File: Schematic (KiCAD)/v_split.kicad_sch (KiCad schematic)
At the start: 109 parts, among them P1 INVERT, P10 NAND_2, P11 NAND_2, P12,13,18,19,25,26 Reg 3 DFF-Reset, P14 INVERT, P15 T-FF Preload, P16 NAND_2, P17 NAND_2, P2 NOR_2, P20 INVERT, P21 T-FF Preload, P22 BUFFER, P23 NAND_2, P24 NAND_2, P28 BUFFER, P3 INVERT, P4 INVERT, P6 Reg 2 DFF-Reset N, P8 INVERT, P9 T-FF Preload, T1 INVERT, T10 INVERT, T12 T-FF Preload, T13 INVERT, T14 INVERT, T15 T-FF Preload, T16 INVERT, T17 INVERT, T18 T-FF Preload, T19 INVERT, T2 INVERT, T20 INVERT, T21 T-FF Preload, T22 INVERT, T23 INVERT, T24 T-FF Preload, T25 INVERT, T26 INVERT, T27 T-FF Preload, T28 INVERT, T29 INVERT, T3 NAND_2, T30 T-FF Preload, T31 INVERT, T4 JK-FF Reset, T5 BUFFER, T6 INVERT, T7 INVERT, T8 T-FF Preload, T9 INVERT, X1 INVERT, X2 NAND_2

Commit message: - Lots of additional comments and signal name improvements.  - "Don't know what this is yet but it is important" section of the pulse channels:    - I worked out the logic and it is a 4-bit binary up-counter with preload, made from gates and D-latches instead of T-flip-flops.    - It is extremely similar to the envelope counter, but takes twice the die space and much more traces.    - None of its outputs go anywhere else, so I believe that it has no actual function.    - It seems to be a previous attempt at making the envelope counter and it got disconnected and left in.    - Each pulse channel has its own copy and I moved both of them to the "Artifacts" sheet.    - The wasted space amounts to about half of one of the large columns on the left side of the die.  - A couple of "OAI2" cells that noted "unclear order": I determined the correct order of the inputs based on several others which were known.  - Deduced the purpose of the 2 separate methods of scanline detection:    - The one looking for 3 consecutive reads finds the start of a scanline.    - The one counting PPU /RD to find PPU cycle 336, finds the end of the scanline.    - I moved these beside each other on the same sheet for clarity.  - A66.5 Changed from Nand to Nor in order to make sense.  - Basic test mode:    - Pin 92: Active low, enables test mode.    - Pin 29: In test mode, it gives external control of "Scanline Start Detection", which is normally done with the familiar 3 matching PPU reads.  When not in test mode, the pin has no function.    - Pin 30: In test mode, it gives external control of "Scanline End Detection", which is normally done by counting PPU /RD to find PPU cycle 336.  It also gives control of "Pulse Length Clock" when in test mode.  When not in test mode, the pin has no function.    - Pin 98/SL3: In test mode, it gives external control of "Pulse Timer Clock".  Whether or not in test mode, this pin low makes the MMC5 pretend $5104 had not yet been written since reset, probably as a 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
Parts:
- removed P1, P3, P4, R7, R8, S5, S6, X1: INVERT, symbol MMC5:INVERT
- removed P2: NOR_2, symbol MMC5:NOR_2
- removed R1: AOI_2, symbol MMC5:AOI_2
- removed R6, X2: NAND_2, symbol MMC5:NAND_2
- removed T4: JK-FF Reset, symbol MMC5:JK-FF_Reset
- removed T5: BUFFER, symbol MMC5:BUFFER
- added N3, N4: NAND_2, symbol MMC5:NAND_2
- added N5: XNOR_2, symbol MMC5:XNOR_2
- added T4: D-FF-SR, symbol MMC5:D-FF-SR
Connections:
- net $5200.6{P6} is gone; now on net /Reset_Detect{N2}: P6. (/Q1)
- net $5200.7{P6} is gone; now on net /Reset_Detect{N2}: P6. (/Q1)
- net +PPU_Fetch_Count.5{S25} is gone; now on net +PPU_Fetch_Counter.7{S29}: S4. (X)
- net Increment_PPU_Fetch_Count{S6} is gone; now on net /Reset_Detect{R14}: R4. (Q1)
- net R4.Q1 is gone; now on net /Reset_Detect{R14}: R4. (Q1)
- net V-Split_Scanline_Detected{P3} is gone; now on net Scanline_End_Detected{P3}: P22. (X), T8. (/Q)
- net V-Split_Scanline_Detected{T5} is gone; now on net Scanline_End_Detected{T5}: T3. (X)
- net V-Split_Side_Being_Rendered{V7} is gone; now on an unnamed net: V7. (X)
- net /PPU_Fetch_Count.4{S23} is gone; now on net /PPU_Fetch_Counter.4{S23}: S3. (X)
- net +PPU_Fetch_Counter.2{S18}: now also S3. (X), S4. (X)
- net +PPU_Fetch_Counter.5{S25}: now also S4. (X)
- net +PPU_Fetch_Counter.7{S29}: now also S3. (X)
- net /V-Split_Scanline=239{S30}: now also T4. (/Q)
- net at V4. (X): now also V5. (X); no longer V6. (X)
- net at V9. (X): now also V11. (X); no longer V4. (X)
- net at R27. (/Q): now also R26. (X)
- net at R26. (X): now also R29. (X); no longer R27. (/Q)
- net at P9. (/Q): now also P8. (X); no longer P10. (X)
- net at T2. (X): now also T1. (X); no longer T3. (X)
- net Scanline_End_Detected{T5}: now reaches T3. (X)
- net Scanline_End_Detected{T5}: now also T4. (/Q)
- net at P28. (X): now also R26. (X); no longer P12,13,18,19,25,26. (Q2)
- net at T20. (X): now also T21. (/Q); no longer V27. (X)
- net at T21. (/Q): now also V28. (X), V29. (X); no longer T20. (X)
- net at P21. (/Q): no longer P22. (X)
- net at T14. (X): now also T15. (/Q); no longer V19. (X)
- net at V7. (X): now also N4. (X); no longer V8. (/Q)
- net at T29. (X): now also V36. (X); no longer T30. (/Q)
- net at P15. (/Q): now also P20. (X), P21. (/Q); no longer P16. (X)
- net at V11. (X): now also V10. (X); no longer V12. (X)
- net at T26. (X): now also T27. (/Q); no longer V33. (X)
- net at T27. (/Q): no longer T26. (X)
- net /PPU_Fetch_Counter.4{S23}: now reaches S3. (X)
- net /PPU_Fetch_Counter.4{S23}: no longer R4. (Q1)
- net at T12. (/Q): now also T8. (/Q), T9. (X)
- net at T10. (X): now also V16. (X); no longer T12. (/Q)
- net at T30. (/Q): now also V37. (X), V38. (X); no longer T31. (X)
- net at T23. (X): now also V30. (X); no longer T24. (/Q)
- net at T15. (/Q): no longer T14. (X)
- net at BH32. (X): now also BH31. (X)
- net at T7. (X): now also T8. (/Q); no longer V13. (X)
- net Scanline_End_Detected{P3}: now reaches T8. (/Q)
- net Scanline_End_Detected{P3}: now also N3. (X); no longer T7. (X)
- net at T18. (/Q): now also T17. (X)
- net at T17. (X): now also V22. (X); no longer T18. (/Q)
- removed net +PPU_Fetch_Count.0{S10}: S3. (X), S4. (X)
- removed net +PPU_Fetch_Count.1{S13}: S3. (X), S4. (X)
- removed net +PPU_Fetch_Count.2{S18}: S3. (X), S4. (X)
- removed net +PPU_Fetch_Count.7{S29}: S3. (X), S4. (X)
- new net: N1. (X), P6. (/Q1)
- new net: V4. (X), V6. (X)
- new net: V3. (X), V4. (X)
- new net: V4. (X), V9. (X)
- new net: R27. (/Q), R28. (X)
- new net: R27. (/Q), R29. (X)
- new net: P10. (X), P9. (/Q)
- new net: P10. (X), P11. (X), P9. (/Q)
- new net: T3. (X), T4. (/Q)
- new net: BH28. (X), T4. (/Q)
- new net: BH32. (X), T4. (/Q)
- new net: T2. (X), T3. (X)
- new net: T18. (/Q), T19. (X), T21. (/Q)
- new net: T15. (/Q), T16. (X), T18. (/Q)
- new net: V6. (X), W2. (Q4)
- new net: P12,13,18,19,25,26. (Q2), P28. (X)
- new net: P12,13,18,19,25,26. (Q2), P17. (X)
- new net: P11. (X), P12,13,18,19,25,26. (Q2)
- new net: P12,13,18,19,25,26. (Q2), P24. (X)
- new net: P14. (X), P15. (/Q), P9. (/Q)
- new net: T20. (X), V27. (X)
- new net: T27. (/Q), V34. (X), V35. (X)
- new net: V33. (X), V34. (X)
- new net: P21. (/Q), P22. (X)
- new net: V19. (X), V20. (X)
- new net: T14. (X), V19. (X)
- new net: V7. (X), V8. (/Q)
- new net: V27. (X), V28. (X)
- new net: V3. (X), W2. (Q4)
- new net: T29. (X), T30. (/Q)
- new net: P15. (/Q), P16. (X), P17. (X)
- new net: P15. (/Q), P16. (X)
- new net: T18. (/Q), V23. (X), V26. (X)
- new net: V26. (X), W3,V24,V25,V41. (Q7)
- new net: V8. (/Q), V9. (X)
- new net: N3. (X), N4. (X), N5. (X)
- new net: V35. (X), W3,V24,V25,V41. (Q7)
- new net: V11. (X), V12. (X)
- new net: V12. (X), W2. (Q4)
- new net: P21. (/Q), P23. (X)
- new net: P21. (/Q), P23. (X), P24. (X)
- new net: T24. (/Q), T25. (X), T27. (/Q)
- new net: T26. (X), V33. (X)
- new net: T15. (/Q), V20. (X), V21. (X)
- new net: R4. (Q1), S4. (X)
- new net: R4. (Q1), S3. (X)
- new net: T12. (/Q), V17. (X), V18. (X)
- new net: T12. (/Q), T13. (X), T15. (/Q)
- new net: T10. (X), T12. (/Q)
- new net: V22. (X), V23. (X)
- new net: V18. (X), W3,V24,V25,V41. (Q7)
- new net: T30. (/Q), T31. (X)
- new net: T23. (X), T24. (/Q)
- new net: T21. (/Q), T22. (X), T24. (/Q)
- new net: BH29. (X), BH30. (X)
- new net: T27. (/Q), T28. (X), T30. (/Q)
- new net: V16. (X), V17. (X)
- new net: T7. (X), V13. (X)
- new net: V13. (X), V14. (X)
- new net: V5. (X), W2. (Q4)
- new net: V36. (X), V37. (X)
- new net: T24. (/Q), V31. (X), V32. (X)
- new net: V32. (X), W3,V24,V25,V41. (Q7)
- new net: V29. (X), W3,V24,V25,V41. (Q7)
- new net: T6. (X), V11. (X)
- new net: V30. (X), V31. (X)
- new net: N3. (X), N4. (X)
- new net: V38. (X), W3,V24,V25,V41. (Q7)
- new net: T8. (/Q), V14. (X), V15. (X)
- new net: V2. (X), W2. (Q4)
- new net: V21. (X), W3,V24,V25,V41. (Q7)
- new net: V15. (X), W3,V24,V25,V41. (Q7)
- new net: V10. (X), W2. (Q4)
- new net +$5200.6_V-Split_Side_Right{P6}: N5. (X), P6. (/Q1)
- new net +$5200.7_V-Split_Enable{P6}: P6. (/Q1)
- new net +PPU_Cycle_336{R4}: R4. (Q1)
- new net +PPU_Fetch_Counter.0{S10}: S3. (X), S4. (X)
- new net +PPU_Fetch_Counter.1{S13}: S3. (X), S4. (X)
- new net Increment_Scanline_Fetch_Count{S6}: R4. (Q1)
- new net PPU_Fetch_Count_Match_0{R4}: R4. (Q1)
- new net V-Split_Rendering{N5}: N5. (X)
- now unconnected: P21. (/Q), P21. (/Q), P21. (/Q), T15. (/Q), T15. (/Q), T15. (/Q), T24. (/Q), T24. (/Q), T24. (/Q), T27. (/Q), T27. (/Q), T27. (/Q)
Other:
- note added: "0=prevent reload 1=allow reload"
- note added: "Comparing the fetch counter, shifted right by 2, to the $5200 V-Split H-threshold, Every 4 fetches = 1 tile. The match at V9..V7 holds true only for 1 fetch, so it is latched by N3/N4 until a new scanline is detected."
- note added: "Q1 = 1 at PPU cycle 336 for incrementing V-split scanline counter. Logic from S4: Value 1x1xx111, when incrementing, First triggered at 10100111=0xA7=167. Because fetch count clocks the latch, 167+1 = 168. Since PPU has 2 cycles per fetch, 168*2=336 cycles. This aligns with "unused NT fetches" at the end of the scanline."
- note added: "S3 = 0 at these values: 135, 143 (cycle 272, 288) 167, 175 (cycle 336, 352) 199, 207 (cycle 400, 416) 231, 239 (cycle 464, 480) These values don't make much sense, but it seems it should correlate to sprite pattern fetches"
- note added: "XNor N5 selects the left/right side based on $5002.6"
- note removed: "I am guessing this is any PPU fetch excluding sprites"
- note removed: "This Flip-Flop is unknown and J & K are complete guesses. May need swapping or inverting J & K and Q & /Q."
- note removed: "This cell has unknown logic"
- moved on the sheet: BH28, BH29, BH30, BH31, BH32, N1, P6, R4, S3, S30, S4

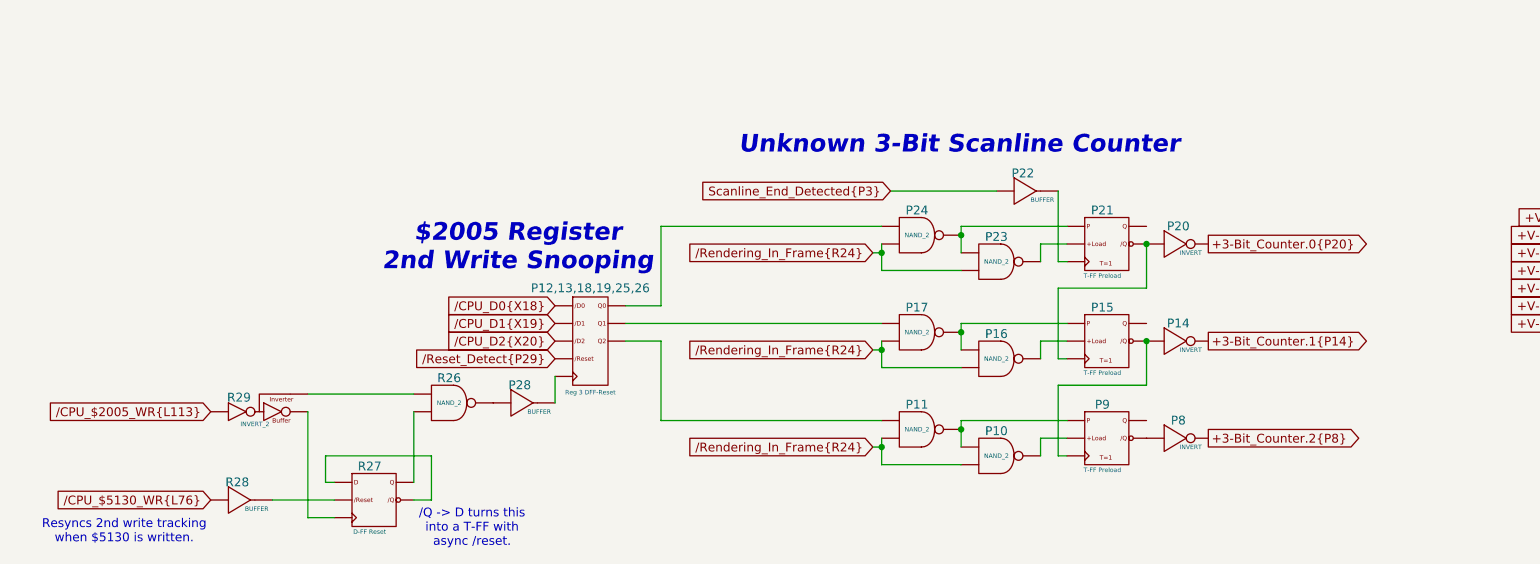
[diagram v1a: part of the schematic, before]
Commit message: I fixed 2 errors in the letterless MMC5 tracing:
1. BK5 is a NAND-4 gate.  It was thought to be NAND-3 before.
2.  BL83 and BL96 signals got swapped here before.  They actually cross each other:

BL83 = "PPU_RW_Mode_%0x_Access"
BL96 = "+ExRAM_Mode_$0x"

This propagated out to several changes in the schematic.
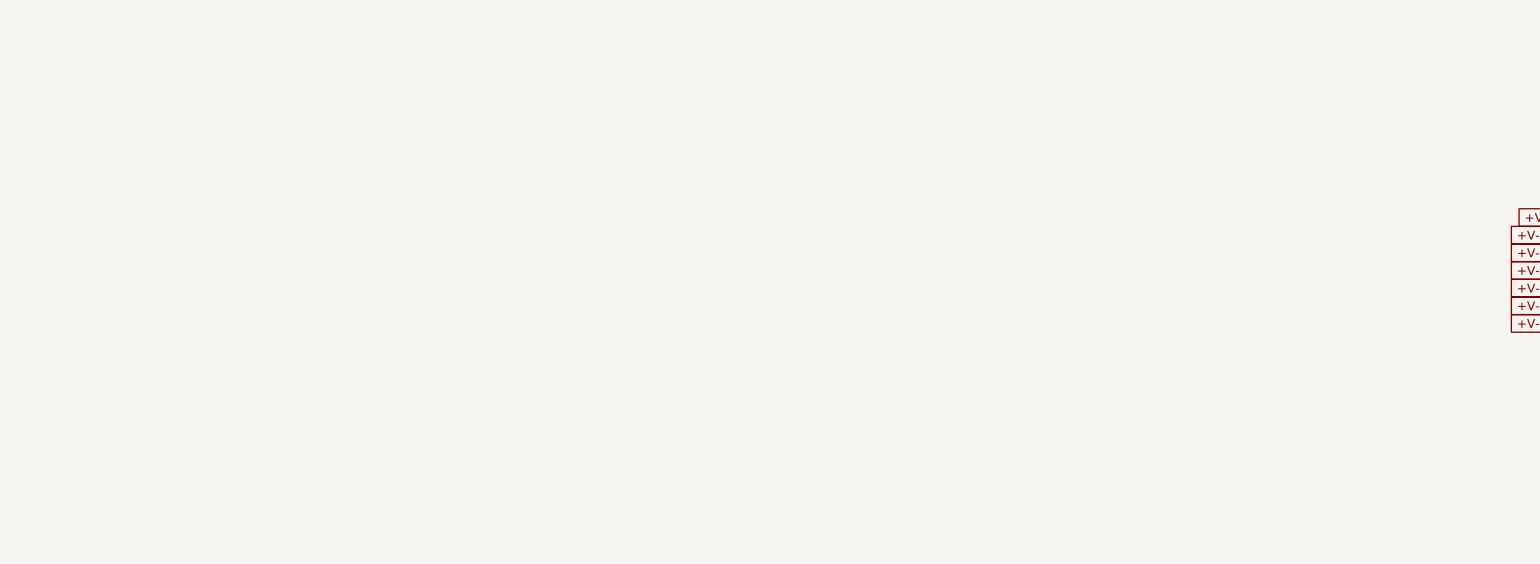
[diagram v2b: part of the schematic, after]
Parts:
- removed P10, P11, P16, P17, P23, P24, R26: NAND_2, symbol MMC5:NAND_2
- removed P12,13,18,19,25,26: Reg 3 DFF-Reset, symbol MMC5:Reg_3_DFF-Reset
- removed P14, P20, P8: INVERT, symbol MMC5:INVERT
- removed P15, P21, P9: T-FF Preload, symbol MMC5:T-FF_Preload
- removed P22, P28, R28: BUFFER, symbol MMC5:BUFFER
- removed R27: D-FF Reset, symbol MMC5:D-FF_Reset
- removed R29: INVERT_2, symbol MMC5:INVERT_2
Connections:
- net at V4. (X): now also V5. (X); no longer V6. (X)
- net at V9. (X): now also V11. (X); no longer V4. (X)
- net at BH28. (X): now also BH29. (X); no longer T4. (/Q)
- net at BH32. (X): now also BH31. (X); no longer T4. (/Q)
- net at T2. (X): now also T1. (X); no longer T3. (X)
- net at T20. (X): now also T21. (/Q); no longer V27. (X)
- net at T21. (/Q): now also V28. (X), V29. (X); no longer T20. (X)
- net at T14. (X): now also T15. (/Q); no longer V19. (X)
- net at V7. (X): now also N4. (X); no longer V8. (/Q)
- net at N4. (X): now also N3. (X); no longer V7. (X)
- net at T29. (X): now also V36. (X); no longer T30. (/Q)
- net at V11. (X): now also V10. (X); no longer V12. (X)
- net at T26. (X): now also T27. (/Q); no longer V33. (X)
- net at T27. (/Q): no longer T26. (X)
- net at T12. (/Q): now also T8. (/Q), T9. (X)
- net at T10. (X): now also V16. (X); no longer T12. (/Q)
- net at T30. (/Q): now also V37. (X), V38. (X); no longer T31. (X)
- net at T23. (X): now also V30. (X); no longer T24. (/Q)
- net at T15. (/Q): no longer T14. (X)
- net at T7. (X): now also T8. (/Q); no longer V13. (X)
- net at T18. (/Q): now also T17. (X)
- net at T17. (X): now also V22. (X); no longer T18. (/Q)
- new net: N1. (X), P6. (/Q1)
- new net: V4. (X), V6. (X)
- new net: V3. (X), V4. (X)
- new net: V4. (X), V9. (X)
- new net: T3. (X), T4. (/Q)
- new net: BH28. (X), T4. (/Q)
- new net: BH32. (X), T4. (/Q)
- new net: T2. (X), T3. (X)
- new net: T18. (/Q), T19. (X), T21. (/Q)
- new net: T15. (/Q), T16. (X), T18. (/Q)
- new net: V6. (X), W2. (Q4)
- new net: T20. (X), V27. (X)
- new net: T27. (/Q), V34. (X), V35. (X)
- new net: V33. (X), V34. (X)
- new net: V19. (X), V20. (X)
- new net: T14. (X), V19. (X)
- new net: V7. (X), V8. (/Q)
- new net: V27. (X), V28. (X)
- new net: V3. (X), W2. (Q4)
- new net: T29. (X), T30. (/Q)
- new net: T18. (/Q), V23. (X), V26. (X)
- new net: V26. (X), W3,V24,V25,V41. (Q7)
- new net: V8. (/Q), V9. (X)
- new net: N3. (X), N4. (X), N5. (X)
- new net: V35. (X), W3,V24,V25,V41. (Q7)
- new net: V11. (X), V12. (X)
- new net: V12. (X), W2. (Q4)
- new net: T24. (/Q), T25. (X), T27. (/Q)
- new net: T26. (X), V33. (X)
- new net: T15. (/Q), V20. (X), V21. (X)
- new net: R4. (Q1), S4. (X)
- new net: R4. (Q1), S3. (X)
- new net: T12. (/Q), V17. (X), V18. (X)
- new net: T12. (/Q), T13. (X), T15. (/Q)
- new net: T10. (X), T12. (/Q)
- new net: V22. (X), V23. (X)
- new net: V18. (X), W3,V24,V25,V41. (Q7)
- new net: T30. (/Q), T31. (X)
- new net: T23. (X), T24. (/Q)
- new net: T21. (/Q), T22. (X), T24. (/Q)
- new net: BH29. (X), BH30. (X)
- new net: T27. (/Q), T28. (X), T30. (/Q)
- new net: V16. (X), V17. (X)
- new net: T7. (X), V13. (X)
- new net: V13. (X), V14. (X)
- new net: V5. (X), W2. (Q4)
- new net: V36. (X), V37. (X)
- new net: T24. (/Q), V31. (X), V32. (X)
- new net: V32. (X), W3,V24,V25,V41. (Q7)
- new net: V29. (X), W3,V24,V25,V41. (Q7)
- new net: T6. (X), V11. (X)
- new net: V30. (X), V31. (X)
- new net: V38. (X), W3,V24,V25,V41. (Q7)
- new net: T8. (/Q), V14. (X), V15. (X)
- new net: V2. (X), W2. (Q4)
- new net: V21. (X), W3,V24,V25,V41. (Q7)
- new net: V15. (X), W3,V24,V25,V41. (Q7)
- new net: V10. (X), W2. (Q4)
- now unconnected: T15. (/Q), T15. (/Q), T15. (/Q), T24. (/Q), T24. (/Q), T24. (/Q), T27. (/Q), T27. (/Q), T27. (/Q)
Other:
- note removed: "$2005 Register 2nd Write Snooping"
- note removed: "/Q -> D turns this into a T-FF with async /reset."
- note removed: "Resyncs 2nd write tracking when $5130 is written."
- note removed: "Unknown 3-Bit Scanline Counter"
